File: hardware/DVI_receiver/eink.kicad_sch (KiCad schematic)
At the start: 4 parts, among them J6 DF12NB(3.0)-30DS-0.5V(51), J7 DF12NB(3.0)-30DS-0.5V(51)

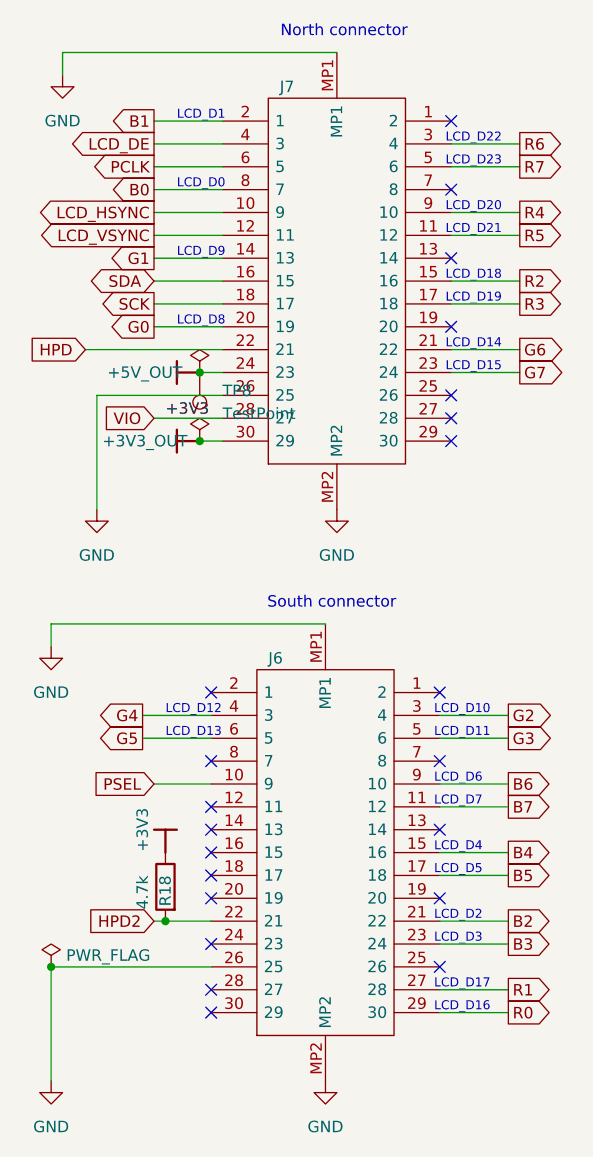
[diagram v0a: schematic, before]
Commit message: fixed mixup of pins G5/G4 (3rd diff pair ODD) and DE/PCLK (3rd diff pair EVEN), now with correct polarity for diff pairs
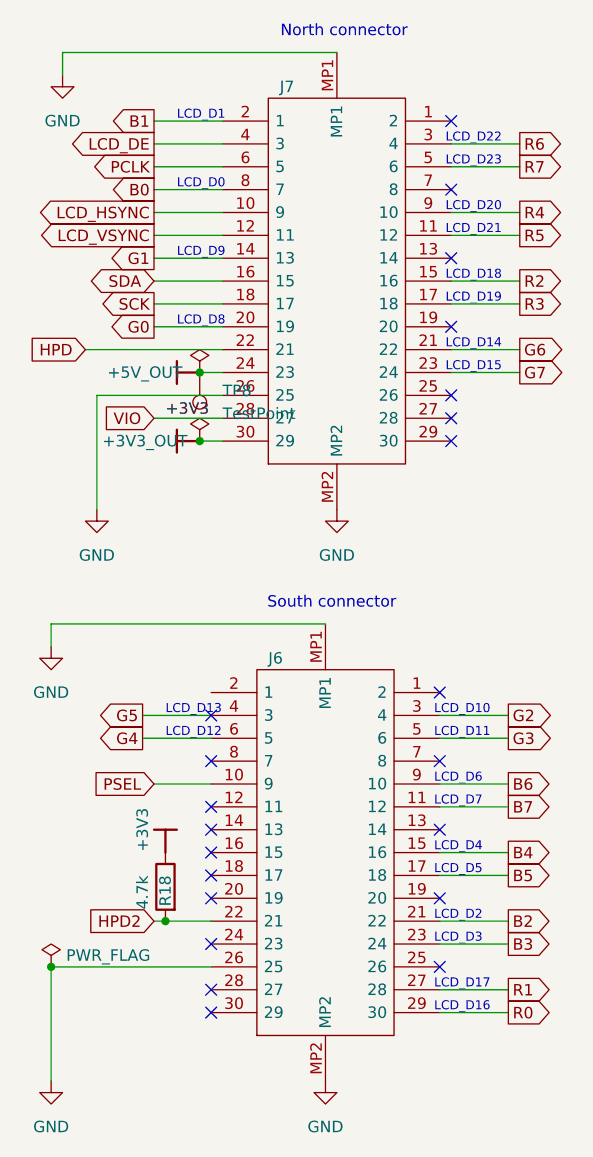
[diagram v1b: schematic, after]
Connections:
- net G4: now also J6.6 (5); no longer J6.4 (3)
- net G5: now also J6.4 (3); no longer J6.6 (5)

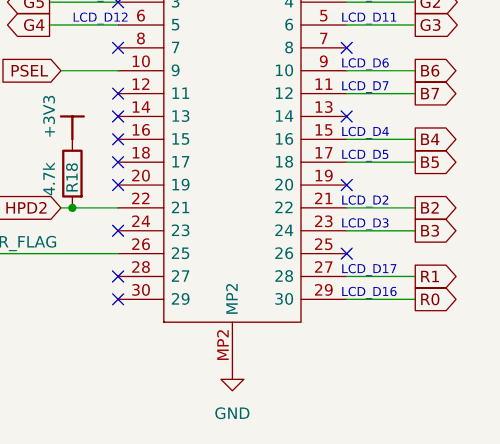
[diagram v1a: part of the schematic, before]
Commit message: fix R0/R1 mixup
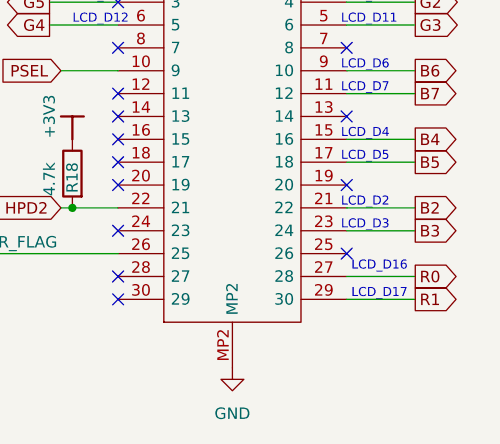
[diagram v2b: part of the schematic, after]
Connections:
- net R0: now also J6.27 (28); no longer J6.29 (30)
- net R1: now also J6.29 (30); no longer J6.27 (28)
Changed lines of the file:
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@@
+		)
+	)
+	(text "LCD_D17"
+		(exclude_from_sim no)
+		(at 65.278 175.26 0)
+		(effects
+			(font
+				(size 1 1)
+			)
+			(justify left bottom)
 		)
 	)
@@
 		)
 	)
-	(text "LCD_D17"
-		(exclude_from_sim no)
-		(at 64.135 172.72 0)
+	(text "LCD_D16"
+		(exclude_from_sim no)
+		(at 65.278 172.212 0)
 		(effects
 			(font
@@
 		(exclude_from_sim no)
 		(at 35.56 91.44 0)
-		(effects
-			(font
-				(size 1 1)
-			)
-			(justify left bottom)
-		)
-	)
-	(text "LCD_D16"
-		(exclude_from_sim no)
-		(at 64.135 175.26 0)
 		(effects
 			(font
@@
 		)
 	)
-	(global_label "R0"
+	(global_label "R3"
+		(shape output)
+		(at 73.66 96.52 0)
+		(fields_autoplaced yes)
+		(effects
+			(font
+				(size 1.27 1.27)
+			)
+			(justify left)
+		)
+		(property "Intersheetrefs" "${INTERSHEET_REFS}"
+			(at 79.1247 96.52 0)
+			(effects
+				(font
+					(size 1.27 1.27)
+				)
+				(justify left)
+				(hide yes)
+			)
+		)
+	)
+	(global_label "SCK"
+		(shape output)
+		(at 33.02 96.52 180)
+		(fields_autoplaced yes)
+		(effects
+			(font
+				(size 1.27 1.27)
+			)
+			(justify right)
+		)
+		(property "Intersheetrefs" "${INTERSHEET_REFS}"
+			(at 26.2853 96.52 0)
+			(effects
+				(font
+					(size 1.27 1.27)
+				)
+				(justify right)
+				(hide yes)
+			)
+		)
+	)
+	(global_label "R1"
 		(shape output)
 		(at 72.39 175.26 0)
@@
 				)
 				(justify left)
-				(hide yes)
-			)
-		)
-	)
-	(global_label "R3"
-		(shape output)
-		(at 73.66 96.52 0)
-		(fields_autoplaced yes)
-		(effects
-			(font
-				(size 1.27 1.27)
-			)
-			(justify left)
-		)
-		(property "Intersheetrefs" "${INTERSHEET_REFS}"
-			(at 79.1247 96.52 0)
-			(effects
-				(font
-					(size 1.27 1.27)
-				)
-				(justify left)
-				(hide yes)
-			)
-		)
-	)
-	(global_label "SCK"
-		(shape output)
-		(at 33.02 96.52 180)
-		(fields_autoplaced yes)
-		(effects
-			(font
-				(size 1.27 1.27)
-			)
-			(justify right)
-		)
-		(property "Intersheetrefs" "${INTERSHEET_REFS}"
-			(at 26.2853 96.52 0)
-			(effects
-				(font
-					(size 1.27 1.27)
-				)
-				(justify right)
 				(hide yes)
 			)
@@
 		)
 	)
+	(global_label "R0"
+		(shape output)
+		(at 72.39 172.72 0)
+		(fields_autoplaced yes)
+		(effects
+			(font
+				(size 1.27 1.27)
+			)
+			(justify left)
+		)
+		(property "Intersheetrefs" "${INTERSHEET_REFS}"
+			(at 77.8547 172.72 0)
+			(effects
+				(font
+					(size 1.27 1.27)
+				)
+				(justify left)
+				(hide yes)
+			)
+		)
+	)
 	(global_label "G2"
 		(shape output)
@@
 				(hide yes)
 			)
-		)
-	)
-	(global_label "R1"
-		(shape output)
-		(at 72.39 172.72 0)
-		(fields_autoplaced yes)
-		(effects
-			(font
-				(size 1.27 1.27)
-			)
-			(justify left)
-		)
-		(property "Intersheetrefs" "${INTERSHEET_REFS}"
-			(at 77.8547 172.72 0)
-			(effects
-				(font
-					(size 1.27 1.27)
-				)
-				(justify left)
-				(hide yes)
-			)
